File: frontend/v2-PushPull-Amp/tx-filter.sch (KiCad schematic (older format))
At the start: 88 parts, among them K10 HK4100, K11 HK4100, K12 HK4100, K13 HK4100, K14 HK4100, K15 HK4100, K2 HK4100, K3 HK4100, K4 HK4100, K5 HK4100, K6 HK4100, K7 HK4100, K8 HK4100, K9 HK4100

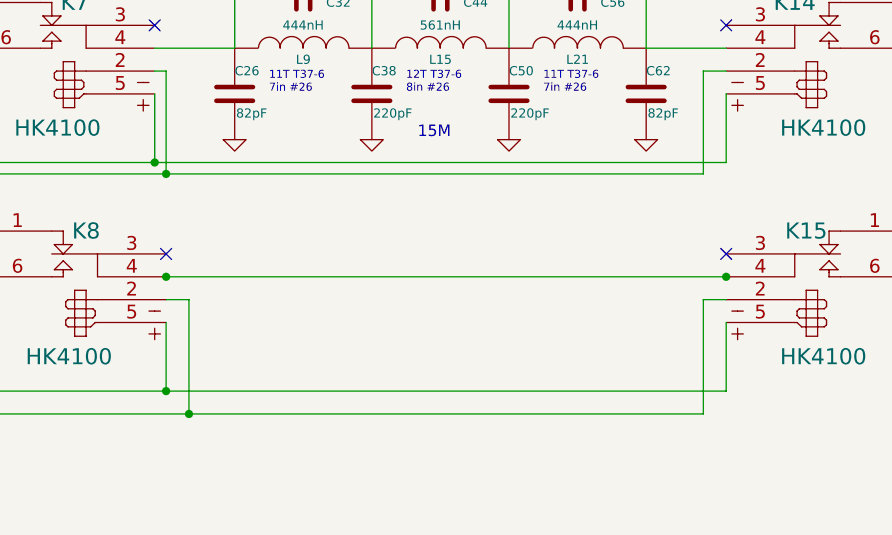
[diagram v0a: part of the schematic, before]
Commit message: Went back to using input transformer with 50R unbalanced input
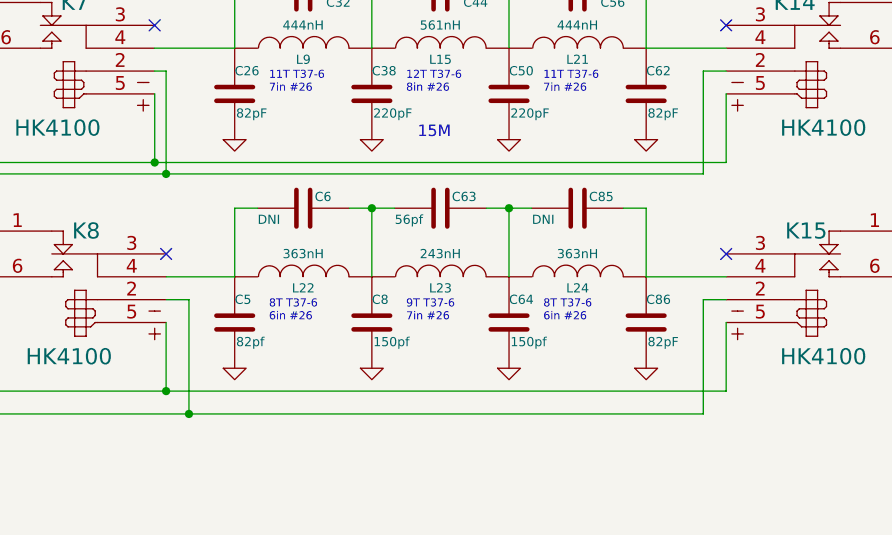
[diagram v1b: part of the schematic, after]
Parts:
- added C5: 82pf, HERMESLITE:C_0805, symbol C-RESCUE-amp
- added C6, C85: DNI, HERMESLITE:C_0805, symbol C-RESCUE-amp
- added C63: 56pf, HERMESLITE:C_0805, symbol C-RESCUE-amp
- added C64, C8: 150pf, HERMESLITE:C_0805, symbol C-RESCUE-amp
- added C86: 82pF, HERMESLITE:C_0805, symbol C-RESCUE-amp
- added L22, L24: 363nH, HERMESLITE:Choke_Toroid, symbol INDUCTOR
- added L23: 243nH, HERMESLITE:Choke_Toroid, symbol INDUCTOR
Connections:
- net GND: now also C5.2, C64.2, C8.2, C86.2
- net at K8.4: now also C5.1, C6.2, L22.1; no longer K15.4
- new net: C85.1, C86.1, K15.4, L24.2
- new net: C6.1, C63.2, C8.1, L22.2, L23.1
- new net: C63.1, C64.1, C85.2, L23.2, L24.1
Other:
- note added: "8T T37-6\n6in #26"
- note added: "9T T37-6\n7in #26"
